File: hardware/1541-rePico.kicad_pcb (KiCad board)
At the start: 2 copper layers, 59.1 x 60 mm, 44 parts, among them IC1 VIA6522, J1 Display Connector, J2 Display Power, J3 Conn_01x05_Pin, J4 SD Card Module Connector, J5 Conn_01x01_Pin, J6 EXT_5V, J7 RESET_1541, J8 Buzzer Connector, P1 VIA_PIN_1-20, P2 VIA_PIN_21-40, Q1 BSS138, Q2 BSS138, Q3 BSS138, Q4 BSS138, Q5 BSS138, Q6 BSS138, Q7 BSS138, Q8 BSS138, Q9 BSS138, SW1 RESET, U1 Pico, U2 SN74LVC4245A

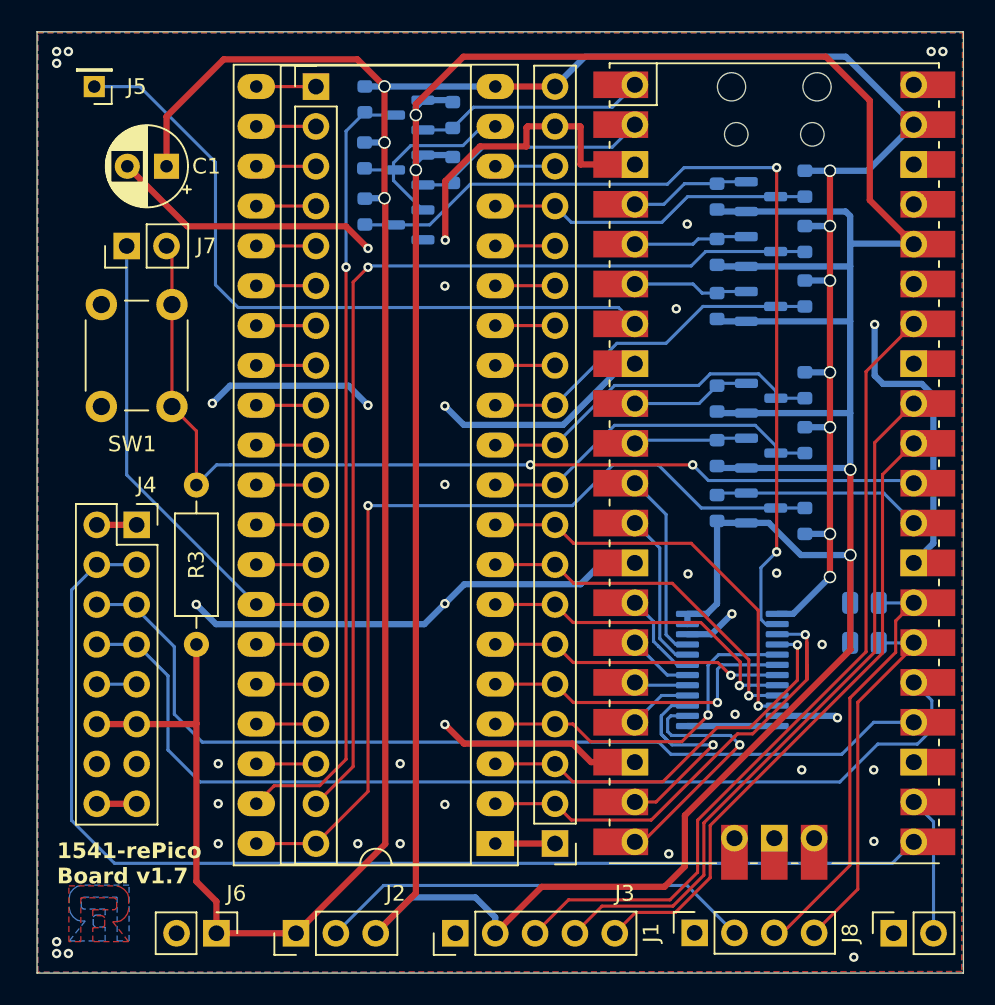
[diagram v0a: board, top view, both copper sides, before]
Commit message: PCB 1.7 fixes and files
updated PCB 1.7 layout:
- rotated SDCard connector
- placed silkscreen text for orientation
- added buzzer-footprint
updated pdf for SCH and PCB files
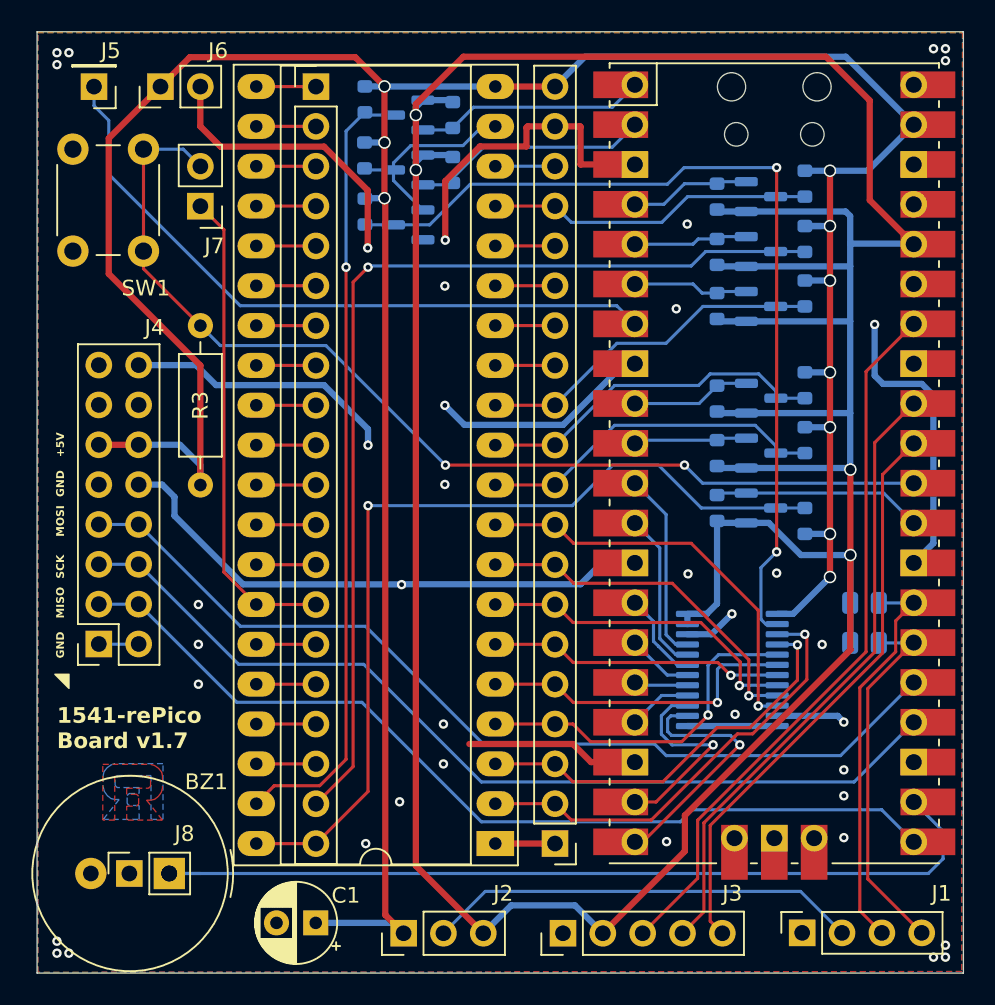
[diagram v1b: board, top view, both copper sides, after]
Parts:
- added BZ1: Buzzer, Buzzer_Beeper:Buzzer_TDK_PS1240P02BT_D12.2mm_H6.5mm, F.Cu at (108.6, 118.7)
- J5: footprint Connector_PinHeader_2.00mm:PinHeader_1x01_P2.00mm_Vertical -> Connector_PinHeader_2.54mm:PinHeader_1x01_P2.54mm_Vertical
- moved J6 54.1 mm to (108.0, 68.6), turned to 90 degrees
- moved C1 49.2 mm to (117.9, 121.9)
- moved J8 48.9 mm to (106.1, 118.7)
- moved R3 10.2 mm to (110.6, 83.8)
- moved SW1 10.1 mm to (102.5, 79.0)
- moved J4 7.97 mm to (104.1, 104.1), turned to 180 degrees
- moved J1 6.86 mm to (149.0, 122.5)
- moved J3 6.86 mm to (133.7, 122.5)
- moved J2 6.86 mm to (123.5, 122.5)
- moved J7 5.34 mm to (110.6, 76.2), turned to 180 degrees
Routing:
- net BUZZER+: track 8.89 -> 56.1 mm
- net MISO: track 74.9 -> 58.9 mm
- net +3.3V: track 241.6 -> 233.9 mm
- net +5V: track 193.7 -> 201.4 mm
- net Net-(J3-Pin_3): track 52.6 -> 46.0 mm
- net Net-(J3-Pin_4): track 45.4 -> 39.9 mm
- net MOSI: track 64.5 -> 60.0 mm
- net Net-(J7-Pin_2): track 62.8 -> 66.5 mm
- net Net-(J3-Pin_5): track 40.6 -> 36.9 mm
- net GND: track 152.1 -> 155.8 mm
- net /VIA 6522 Sockel/PA0: track 32.0 -> 28.7 mm
- net I2C_SCL: track 27.3 -> 25.3 mm
- net /_PA6: track 15.1 -> 13.2 mm
- net Net-(J5-Pin_1): track 45.3 -> 43.5 mm
- net /VIA 6522 Sockel/~{RESET}: track 30.1 -> 30.7 mm
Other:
- board text added: "+5V"
- board text added: "GND"
- board text added: "MISO"
- board text added: "MOSI"
- board text added: "SCK"

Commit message: update PCB to V1.7.0
added jumper-selector for SD-Card VCC (3.3V vs 5V)
slight movements of Buzzer, SDCard-header
changed Footprint of Buzzer to fit passive Buzzer-pin distance
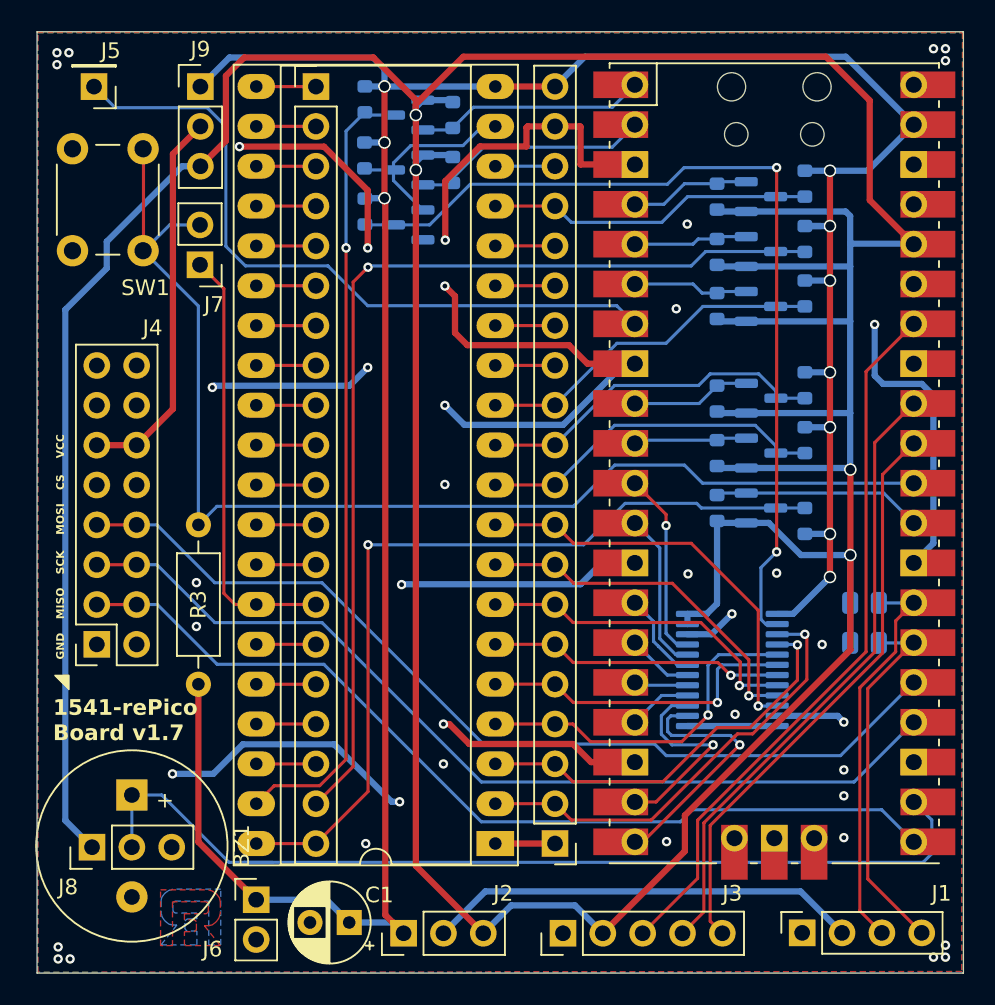
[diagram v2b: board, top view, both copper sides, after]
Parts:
- added J9: SD Power, Connector_PinHeader_2.54mm:PinHeader_1x03_P2.54mm_Vertical, F.Cu at (110.6, 68.6)
- BZ1: footprint Buzzer_Beeper:Buzzer_TDK_PS1240P02BT_D12.2mm_H6.5mm -> Buzzer_Beeper:MagneticBuzzer_StarMicronics_QMX
- J8: footprint Connector_PinSocket_2.54mm:PinSocket_1x02_P2.54mm_Vertical -> Connector_PinHeader_2.54mm:PinHeader_1x03_P2.54mm_Vertical
- moved J6 52.2 mm to (114.1, 120.4), turned to 0 degrees
- moved R3 12.7 mm to (110.5, 96.5)
- moved BZ1 5.54 mm to (106.2, 113.7), turned to -90 degrees
- moved J7 3.73 mm to (110.6, 79.9)
- moved J8 2.91 mm to (103.7, 117.0)
- moved C1 2.13 mm to (120.1, 121.8)
- moved J4 0.13 mm to (104.0, 104.1)
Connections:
- J4 pad 11: +5V -> Net-(J4-Pin_11)
- J4 pad 12: +5V -> Net-(J4-Pin_11)
- J8 pad 1: GND -> +3.3V
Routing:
- net +3.3V: track 233.9 -> 303.6 mm
- net Net-(J4-Pin_11): track 0.00 -> 24.5 mm
- net +5V: track 201.4 -> 182.6 mm
- net Net-(J7-Pin_2): track 66.5 -> 77.4 mm, vias 2 -> 0
- net BUZZER+: track 56.1 -> 61.9 mm
- net /VIA 6522 Sockel/BRDY: track 56.8 -> 53.3 mm
- net /VIA 6522 Sockel/~{RESET}: track 30.7 -> 27.7 mm
- net Net-(J5-Pin_1): track 43.5 -> 45.2 mm
- net GND: track 155.8 -> 155.2 mm, vias 39 -> 41
- net /_PA0: vias 0 -> 1
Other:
- board text added: "CS"
- board text added: "VCC"
- board text removed: "+5V"

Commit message: pcb V1.7.0 small changes, updated bom
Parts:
- moved J6 52.3 mm to (106.8, 68.6)
- moved J4 2.54 mm to (104.0, 106.7)
- moved C1 2.18 mm to (117.9, 121.8)
- moved SW1 2.06 mm to (102.5, 81.1)
- moved BZ1 1.86 mm to (106.3, 115.6)
- moved J8 1.86 mm to (103.7, 118.9)
- moved J5 0.84 mm to (103.0, 68.6), turned to 0 degrees
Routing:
- net GND: track 155.2 -> 169.5 mm
- net +5V: track 182.6 -> 185.5 mm
- net Net-(J4-Pin_11): track 24.5 -> 27.1 mm
- net BUZZER+: track 61.9 -> 59.9 mm
- net Net-(J7-Pin_2): track 77.4 -> 76.2 mm
- net +3.3V: track 303.6 -> 304.7 mm
- net SCK: track 59.4 -> 58.3 mm
- net MISO: track 59.0 -> 57.9 mm
- net MOSI: track 60.1 -> 59.1 mm
